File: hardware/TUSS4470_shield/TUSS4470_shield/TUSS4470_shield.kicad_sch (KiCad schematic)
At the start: 35 parts, among them J1 VIN, J2 TRANSDUCER, J3 Conn_01x10_Socket, J4 VCC SELECT, J5 Conn_01x08_Socket, J6 Conn_01x06_Socket, J7 Conn_01x08_Socket, SW1 RST, U1 TUSS4470TRTJR

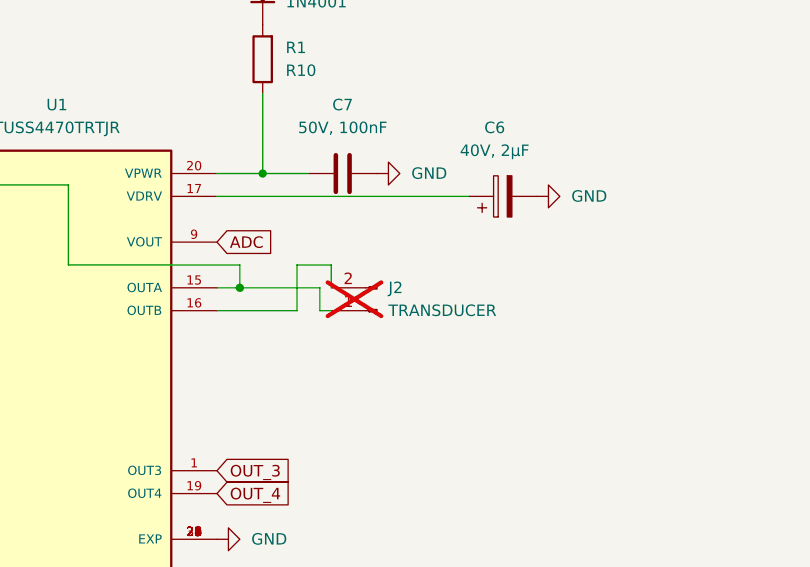
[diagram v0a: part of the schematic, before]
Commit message: fixed fooprint c3 and minor design changes
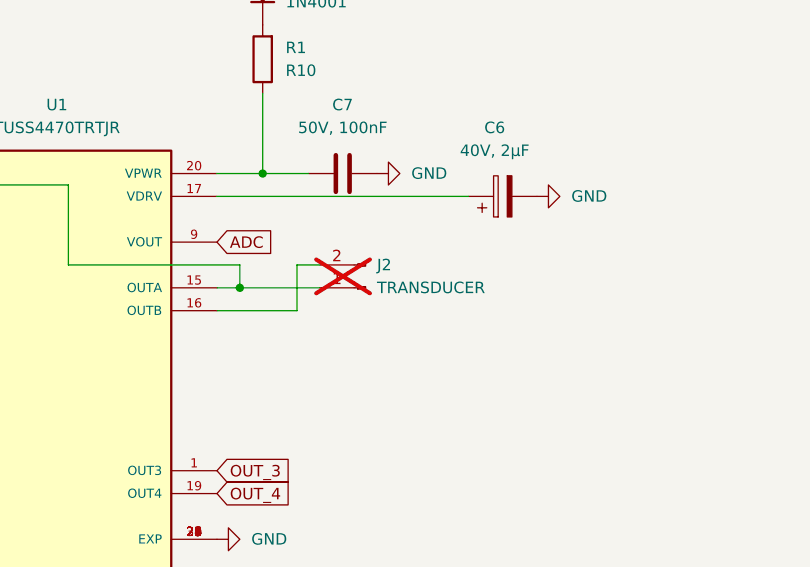
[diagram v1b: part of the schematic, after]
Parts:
- C3: footprint Capacitor_SMD:C_0201_0603Metric -> Capacitor_SMD:C_0603_1608Metric
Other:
- moved on the sheet: J2
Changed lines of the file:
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@@
 	(wire
 		(pts
-			(xy 149.86 69.85) (xy 149.86 72.39)
-		)
-		(stroke
-			(width 0)
-			(type default)
-		)
-	)
-	(wire
-		(pts
 			(xy 102.87 72.39) (xy 71.12 72.39)
 		)
@@
 	(wire
 		(pts
-			(xy 229.87 46.99) (xy 229.87 52.07)
+			(xy 140.97 69.85) (xy 149.86 69.85)
 		)
 		(stroke
@@
 	(wire
 		(pts
-			(xy 217.17 109.22) (xy 227.33 109.22)
+			(xy 229.87 46.99) (xy 229.87 52.07)
 		)
 		(stroke
@@
 	(wire
 		(pts
-			(xy 252.73 86.36) (xy 261.62 86.36)
+			(xy 217.17 109.22) (xy 227.33 109.22)
 		)
 		(stroke
@@
 	(wire
 		(pts
-			(xy 223.52 116.84) (xy 223.52 111.76)
+			(xy 252.73 86.36) (xy 261.62 86.36)
 		)
 		(stroke
@@
 	(wire
 		(pts
-			(xy 149.86 72.39) (xy 151.13 72.39)
+			(xy 223.52 116.84) (xy 223.52 111.76)
 		)
 		(stroke
@@
 	(wire
 		(pts
-			(xy 151.13 67.31) (xy 147.32 67.31)
+			(xy 149.86 67.31) (xy 147.32 67.31)
 		)
 		(stroke
@@
 	(wire
 		(pts
-			(xy 140.97 69.85) (xy 149.86 69.85)
-		)
-		(stroke
-			(width 0)
-			(type default)
-		)
-	)
-	(wire
-		(pts
 			(xy 77.47 69.85) (xy 80.01 69.85)
 		)
@@
 	(wire
 		(pts
-			(xy 151.13 69.85) (xy 151.13 67.31)
-		)
-		(stroke
-			(width 0)
-			(type default)
-		)
-	)
-	(wire
-		(pts
 			(xy 217.17 88.9) (xy 227.33 88.9)
 		)
@@
 	(symbol
 		(lib_id "Connector:Conn_01x02_Pin")
-		(at 156.21 72.39 180)
+		(at 154.94 69.85 180)
 		(unit 1)
 		(exclude_from_sim yes)
@@
 		(fields_autoplaced yes)
 		(property "Reference" "J2"
-			(at 157.48 69.8499 0)
+			(at 156.21 67.3099 0)
 			(effects
 				(font
@@
 		)
 		(property "Value" "TRANSDUCER"
-			(at 157.48 72.3899 0)
+			(at 156.21 69.8499 0)
 			(effects
 				(font
@@
 		)
 		(property "Footprint" "TerminalBlock_4Ucon:TerminalBlock_4Ucon_1x02_P3.50mm_Horizontal"
-			(at 156.21 72.39 0)
+			(at 154.94 69.85 0)
 			(effects
 				(font
@@
 		)
 		(property "Datasheet" "~"
-			(at 156.21 72.39 0)
+			(at 154.94 69.85 0)
 			(effects
 				(font
@@
 		)
 		(property "Description" "Generic connector, single row, 01x02, script generated"
-			(at 156.21 72.39 0)
+			(at 154.94 69.85 0)
 			(effects
 				(font
@@
 			)
 		)
-		(property "Footprint" "Capacitor_SMD:C_0201_0603Metric"
+		(property "Footprint" "Capacitor_SMD:C_0603_1608Metric"
 			(at 96.2152 116.84 0)
 			(effects
